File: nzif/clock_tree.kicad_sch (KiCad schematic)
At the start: 63 parts, among them J1 SMA, U1 AD9523-1BCPZ, U2 SN74AUC16374DGGR, U3 SN74LVC8T245, U4 SN74CBTLV3253, U5 SN74CBTLV3253, U6 SN74LVC8T245, U7 ABLNO-VCXO, X1 CTS_535_TCXO

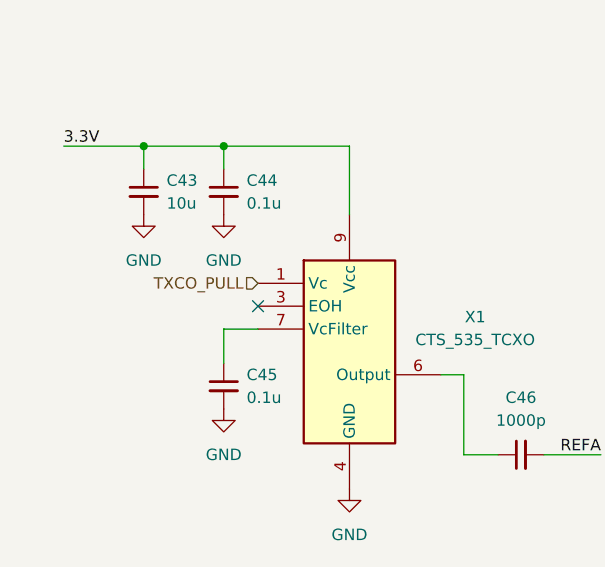
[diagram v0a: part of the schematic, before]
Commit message: added additional control functions ot uC
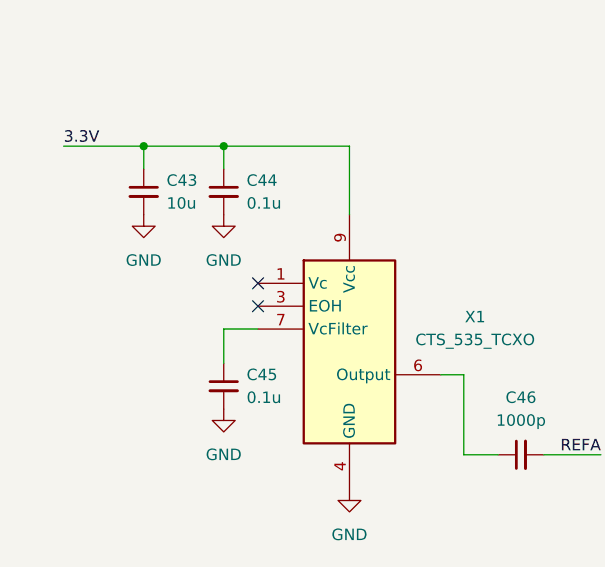
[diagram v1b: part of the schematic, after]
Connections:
- net TXCO_PULL: no longer names the net of X1.1 (Vc)
- no-connect marks 30 -> 31
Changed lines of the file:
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@@
 	)
 	(no_connect
+		(at 45.72 119.38)
+	)
+	(no_connect
 		(at 377.19 201.93)
 	)
@@
 		)
 	)
-	(hierarchical_label "TXCO_PULL"
-		(shape input)
-		(at 45.72 119.38 180)
-		(effects
-			(font
-				(size 1.27 1.27)
-			)
-			(justify right)
-		)
-	)

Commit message: add annotations - first run of erc
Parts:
- renumbered C18 to C233, C29 to C234, C43 to C235, C41 to C236, C19 to C237, C30 to C238, C44 to C239, C45 to C240, C42 to C241, C20 to C242, C31 to C243, C21 to C244, C32 to C245, C22 to C246, C33 to C247, C23 to C248, C34 to C249, C47 to C250, C46 to C251, C48 to C252, C49 to C253, C24 to C254, C35 to C255, C39 to C256, C25 to C257, C36 to C258, C26 to C259, C27 to C260, C28 to C261, C37 to C262, C38 to C263, C3 to C264, C40 to C265, C4 to C266, C5 to C267, C6 to C268, C7 to C269, C10 to C270, C11 to C271, C12 to C272, C13 to C273, C14 to C274, C1 to C275, C8 to C276, C15 to C277, C2 to C278, C9 to C279, C16 to C280, C17 to C281, J1 to J111, R3 to R181, R4 to R182, R2 to R183, R1 to R184, TR1 to TR103, U7 to U128, U1 to U129, U2 to U130, U3 to U131, U4 to U132, U5 to U133, U6 to U134, X1 to X101

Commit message: updated power on all schematics
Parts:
- renumbered C275 to C1, C270 to C10, C271 to C11, C272 to C12, C273 to C13, C274 to C14, C277 to C15, C280 to C16, C281 to C17, C233 to C18, C237 to C19, C278 to C2, C242 to C20, C244 to C21, C246 to C22, C248 to C23, C254 to C24, C257 to C25, C259 to C26, C260 to C27, C261 to C28, C234 to C29, C264 to C3, C238 to C30, C243 to C31, C245 to C32, C247 to C33, C249 to C34, C255 to C35, C258 to C36, C262 to C37, C263 to C38, C256 to C39, C266 to C4, C265 to C40, C236 to C41, C241 to C42, C235 to C43, C239 to C44, C240 to C45, C251 to C46, C250 to C47, C252 to C48, C253 to C49, C267 to C5, C268 to C6, C269 to C7, C276 to C8, C279 to C9, J111 to J1, R184 to R1, R183 to R2, R181 to R3, R182 to R4, TR103 to TR1, U129 to U1, U130 to U2, U131 to U3, U132 to U4, U133 to U5, U134 to U6, U128 to U7, X101 to X1
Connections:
- net 1.8V renamed +1.8V_CLOCKTREE
- net 3.3V renamed +3.3V_CLOCKTREE

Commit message: fixed power on clocktree
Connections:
- net LDO_VCO: no longer C39.1
- net 2.5V renamed +2.5V_CLOCKTREE
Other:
- moved on the sheet: C37, C38, C39, C40, C47, C49, U1A

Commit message: added note to clock tree
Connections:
- net 5V: no longer C16.1, C17.1, U6.23 (V_{CCB}), U6.24 (V_{CCB})
- new net 3V: C16.1, C17.1, U6.23 (V_{CCB}), U6.24 (V_{CCB})
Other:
- note added: "Rx switches are 5V"
- note added: "Tx switches are 3V"
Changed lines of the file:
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@@
 		(company "Andy McCann KA3KAF and Doug McCann KA3KAG")
 	)
+	(rectangle
+		(start 12.7 12.7)
+		(end 73.66 41.91)
+		(stroke
+			(width 0)
+			(type dash)
+		)
+		(fill
+			(type none)
+		)
+	)
+	(text "Rx switches are 5V"
+		(exclude_from_sim no)
+		(at 296.672 17.78 0)
+		(effects
+			(font
+				(size 1.27 1.27)
+			)
+		)
+	)
+	(text "Tx switches are 3V"
+		(exclude_from_sim no)
+		(at 395.732 17.78 0)
+		(effects
+			(font
+				(size 1.27 1.27)
+			)
+		)
+	)
 	(text "1Q8"
 		(exclude_from_sim no)
@@
 		)
 	)
-	(label "5V"
+	(label "3V"
 		(at 408.94 20.32 180)
 		(effects

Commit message: cartoons on main2
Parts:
- renumbered C18 to C233, C29 to C234, C43 to C235, C41 to C236, C19 to C237, C30 to C238, C44 to C239, C45 to C240, C42 to C241, C20 to C242, C31 to C243, C21 to C244, C32 to C245, C22 to C246, C33 to C247, C23 to C248, C34 to C249, C47 to C250, C46 to C251, C48 to C252, C49 to C253, C24 to C254, C35 to C255, C39 to C256, C25 to C257, C36 to C258, C26 to C259, C27 to C260, C28 to C261, C37 to C262, C38 to C263, C3 to C264, C40 to C265, C4 to C266, C5 to C267, C6 to C268, C7 to C269, C10 to C270, C11 to C271, C12 to C272, C13 to C273, C14 to C274, C1 to C275, C8 to C276, C15 to C277, C2 to C278, C9 to C279, C16 to C280, C17 to C281, J1 to J111, R3 to R181, R4 to R182, R2 to R183, R1 to R184, TR1 to TR103, U7 to U128, U1 to U129, U2 to U130, U3 to U131, U4 to U132, U5 to U133, U6 to U134, X1 to X101
